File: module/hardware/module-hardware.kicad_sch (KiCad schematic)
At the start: 49 parts

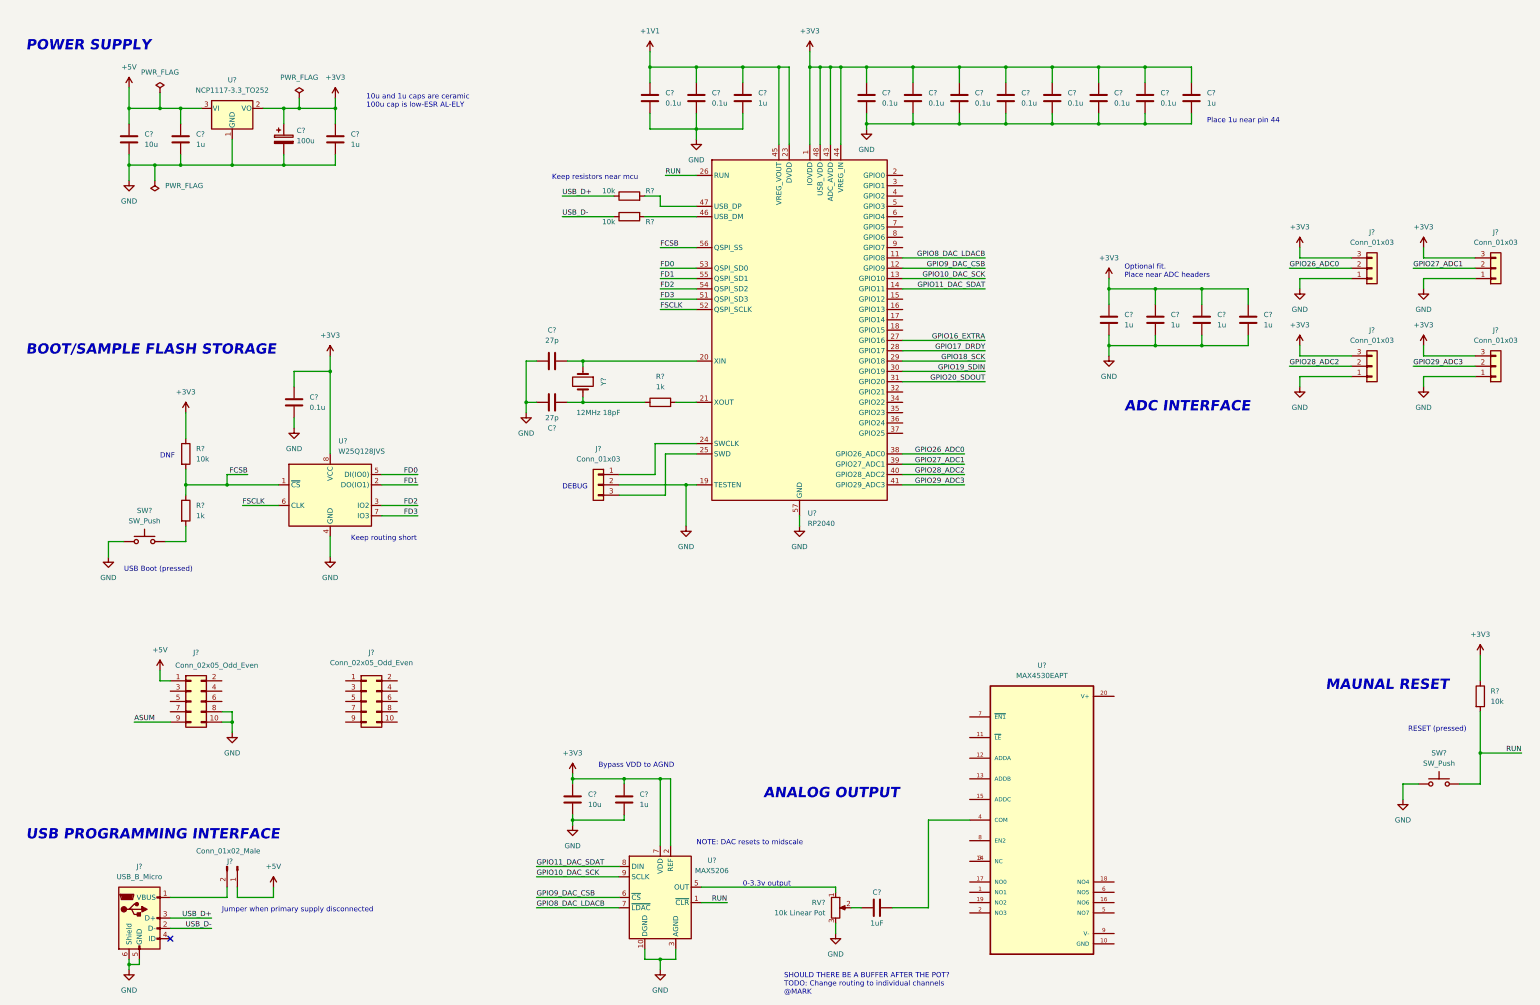
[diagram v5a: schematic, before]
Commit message: Isolated Analog & Digital GND
Also added coupling caps to sequencer mixer
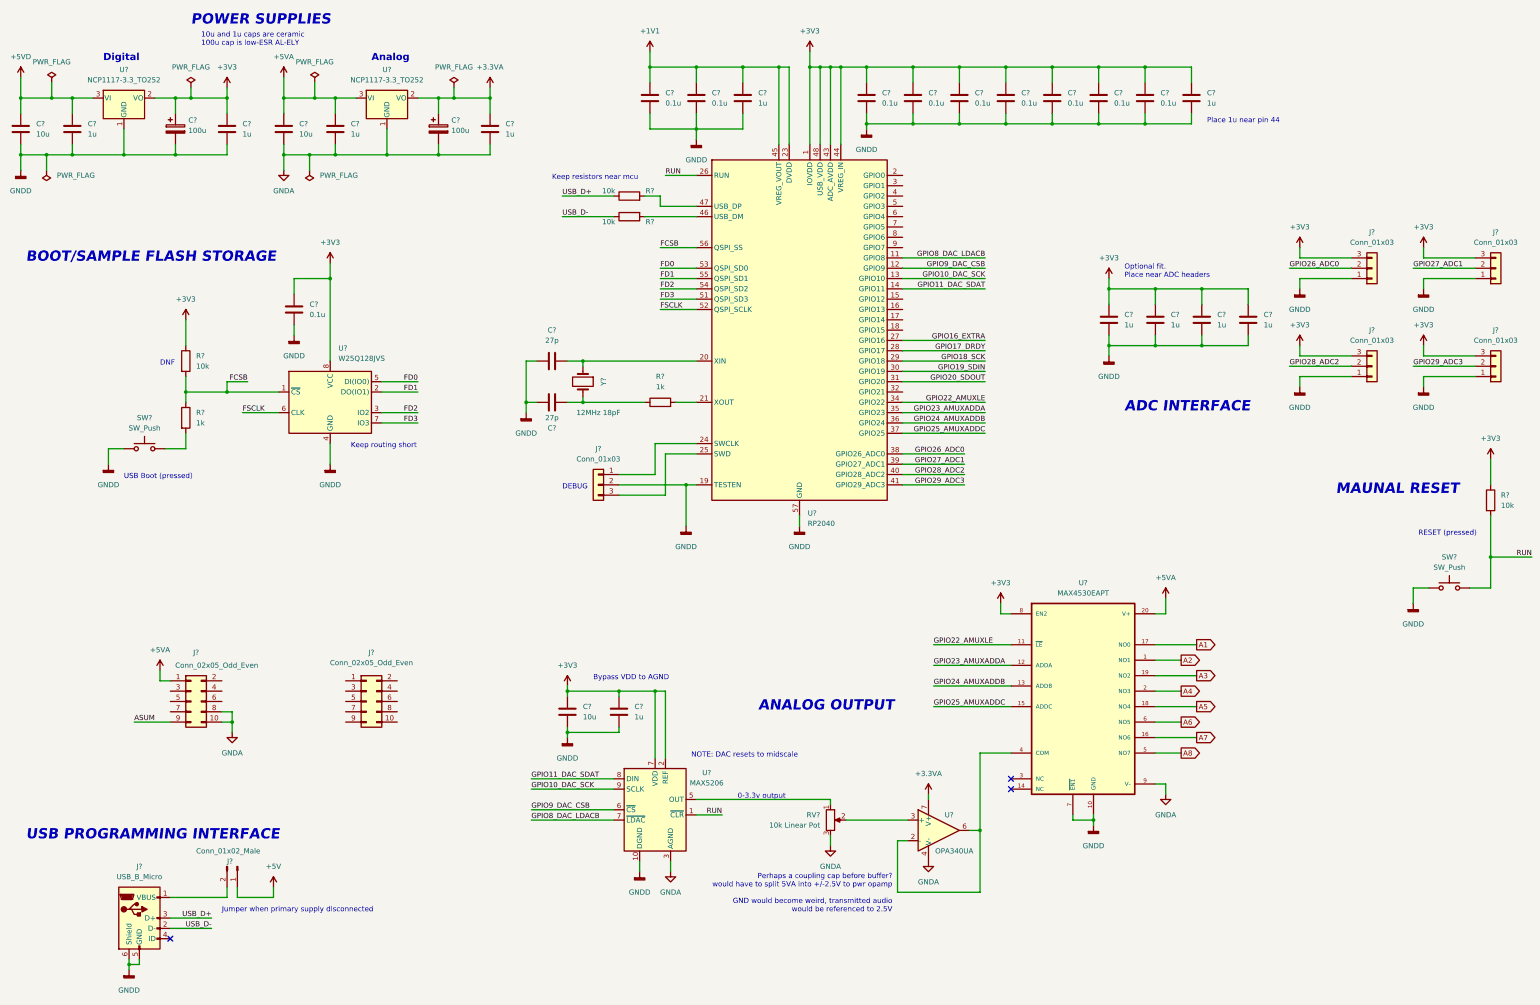
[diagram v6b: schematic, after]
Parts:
- removed C?: 1uF, symbol Device:C
- added C?: 100u, symbol Device:C_Polarized
- added C? (x2): 1u, symbol Device:C
- added C?: 10u, symbol Device:C
- added U?: NCP1117-3.3_TO252, Package_TO_SOT_SMD:TO-252-2, symbol Regulator_Linear:NCP1117-3.3_TO252
- added U?: OPA340UA, Package_SO:SOIC-8_3.9x4.9mm_P1.27mm, symbol Amplifier_Operational:OPA340UA
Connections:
- net +3V3: now also U?.8 (EN2)
- net +5V: no longer C?.1, C?.1, J?.1 (Pin_1), U?.3 (VI)
- net A2: now reaches U?.1 (NO1)
- net GNDD: now reaches U?.10 (GND)
- net GNDD: now also C?.1, C?.2, C?.2, C?.2, C?.2, C?.2, C?.2, C?.2, C?.2, C?.2, C?.2, C?.2, C?.2, C?.2, C?.2, C?.2, C?.2, C?.2, C?.2, C?.2, C?.2, C?.2, C?.2, C?.2, J?.1 (Pin_1), J?.1 (Pin_1), J?.1 (Pin_1), J?.1 (Pin_1), J?.2 (Pin_2), J?.5 (GND), J?.6 (Shield), SW?.1, SW?.1, U?.1 (GND), U?.10 (DGND), U?.19 (TESTEN), U?.4 (GND), U?.57 (GND), U?.7 (~{EN1})
- net GPIO22_AMUXLE: now reaches U?.11 (~{LE})
- net GPIO22_AMUXLE: now also U?.34 (GPIO22)
- net GPIO23_AMUXADDA: now reaches U?.12 (ADDA)
- net GPIO23_AMUXADDA: now also U?.35 (GPIO23)
- net GPIO24_AMUXADDB: now reaches U?.13 (ADDB)
- net GPIO24_AMUXADDB: now also U?.36 (GPIO24)
- net at U?.14 (NC): no longer U?.3 (NC)
- net GPIO25_AMUXADDC: now reaches U?.15 (ADDC)
- net GPIO25_AMUXADDC: now also U?.37 (GPIO25)
- net A7: now reaches U?.16 (NO6)
- net A1: now reaches U?.17 (NO0)
- net A5: now reaches U?.18 (NO4)
- net A3: now reaches U?.19 (NO2)
- net A4: now reaches U?.2 (NO3)
- net +5VA: now reaches U?.20 (V+)
- net +5VA: now also J?.1 (Pin_1), C?.1, C?.1, U?.3 (VI)
- net at U?.4 (COM): now also U?.2 (-), U?.6
- net A8: now reaches U?.5 (NO7)
- net A6: now reaches U?.6 (NO5)
- net GNDA: now reaches U?.9 (V-)
- net GNDA: now also J?.10 (Pin_10), J?.8 (Pin_8), RV?.3, U?.3 (AGND), C?.2, C?.2, C?.2, C?.2, U?.1 (GND), U?.4 (V-)
- net at RV?.2: now also U?.3 (+)
- removed net GND: C?.1, C?.2, C?.2, C?.2, C?.2, C?.2, C?.2, C?.2, C?.2, C?.2, C?.2, C?.2, C?.2, C?.2, C?.2, C?.2, C?.2, C?.2, C?.2, C?.2, C?.2, C?.2, C?.2, C?.2, J?.1 (Pin_1), J?.1 (Pin_1), J?.1 (Pin_1), J?.1 (Pin_1), J?.10 (Pin_10), J?.2 (Pin_2), J?.5 (GND), J?.6 (Shield), J?.8 (Pin_8), RV?.3, SW?.1, SW?.1, U?.1 (GND), U?.10 (DGND), U?.19 (TESTEN), U?.3 (AGND), U?.4 (GND), U?.57 (GND)
- new net +3.3VA: C?.1, C?.1, U?.2 (VO), U?.7 (V+)
- new net +5VD: C?.1, C?.1, U?.3 (VI)
- no-connect marks 1 -> 3
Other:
- note added: "Analog"
- note added: "Digital"
- note added: "POWER SUPPLIES"
- note added: "Perhaps a coupling cap before buffer? would have to split 5VA into +/-2.5V to pwr opamp GND would become weird, transmitted audio would be referenced to 2.5V"
- note removed: "POWER SUPPLY"
- note removed: "SHOULD THERE BE A BUFFER AFTER THE POT? TODO: Change routing to individual channels @MARK"
- moved on the sheet: C?, R?, RV?, SW?, U?

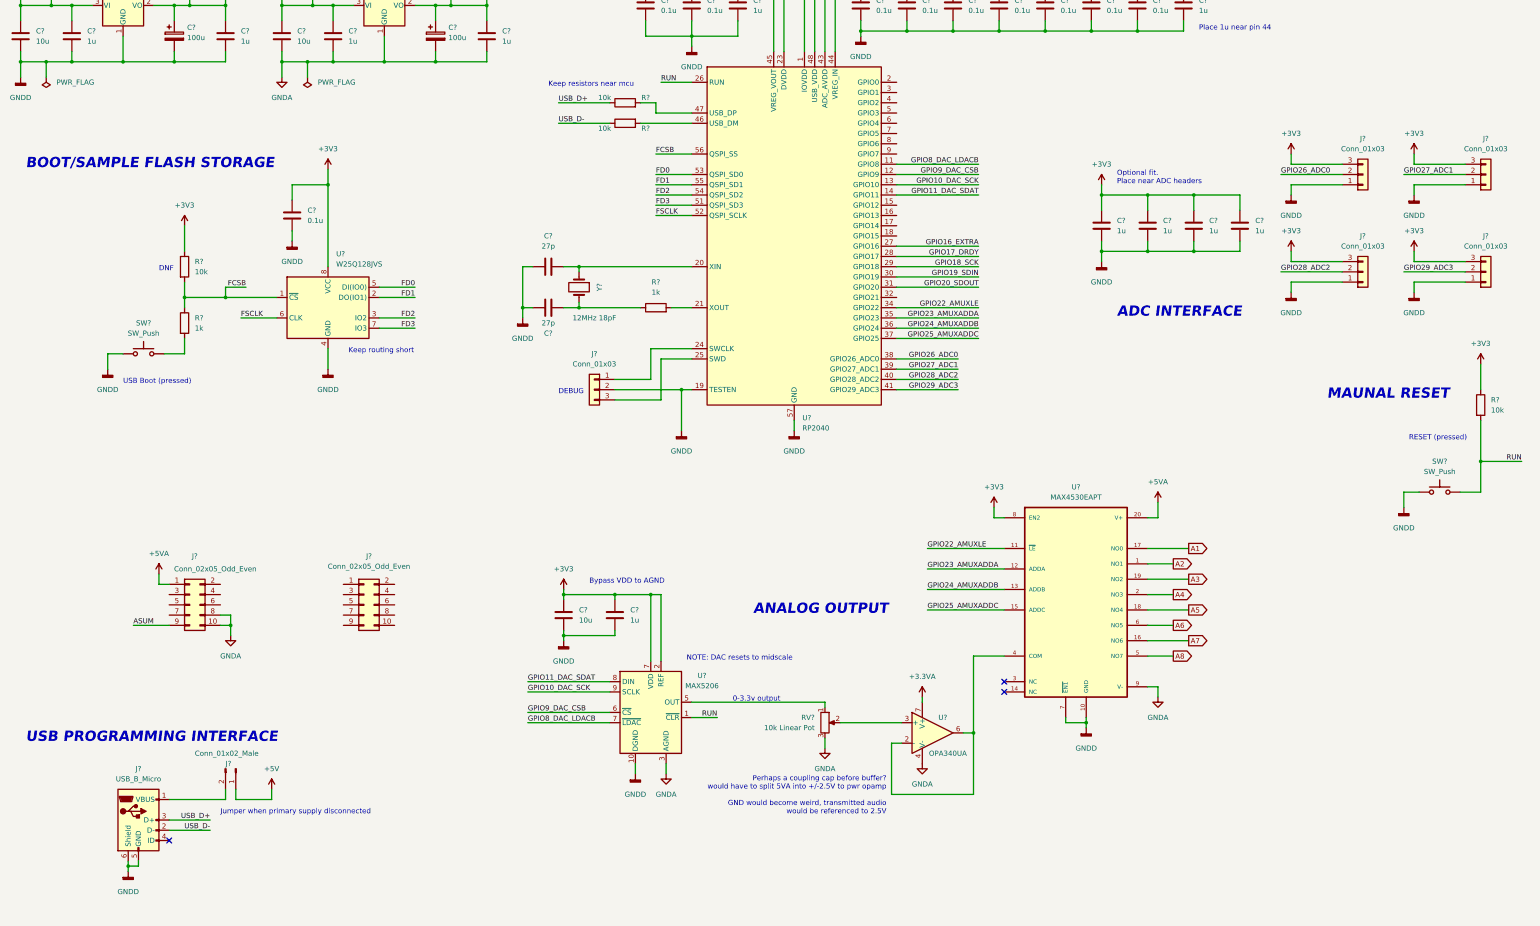
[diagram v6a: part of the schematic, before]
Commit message: Reworked audio routing to avoid MUX
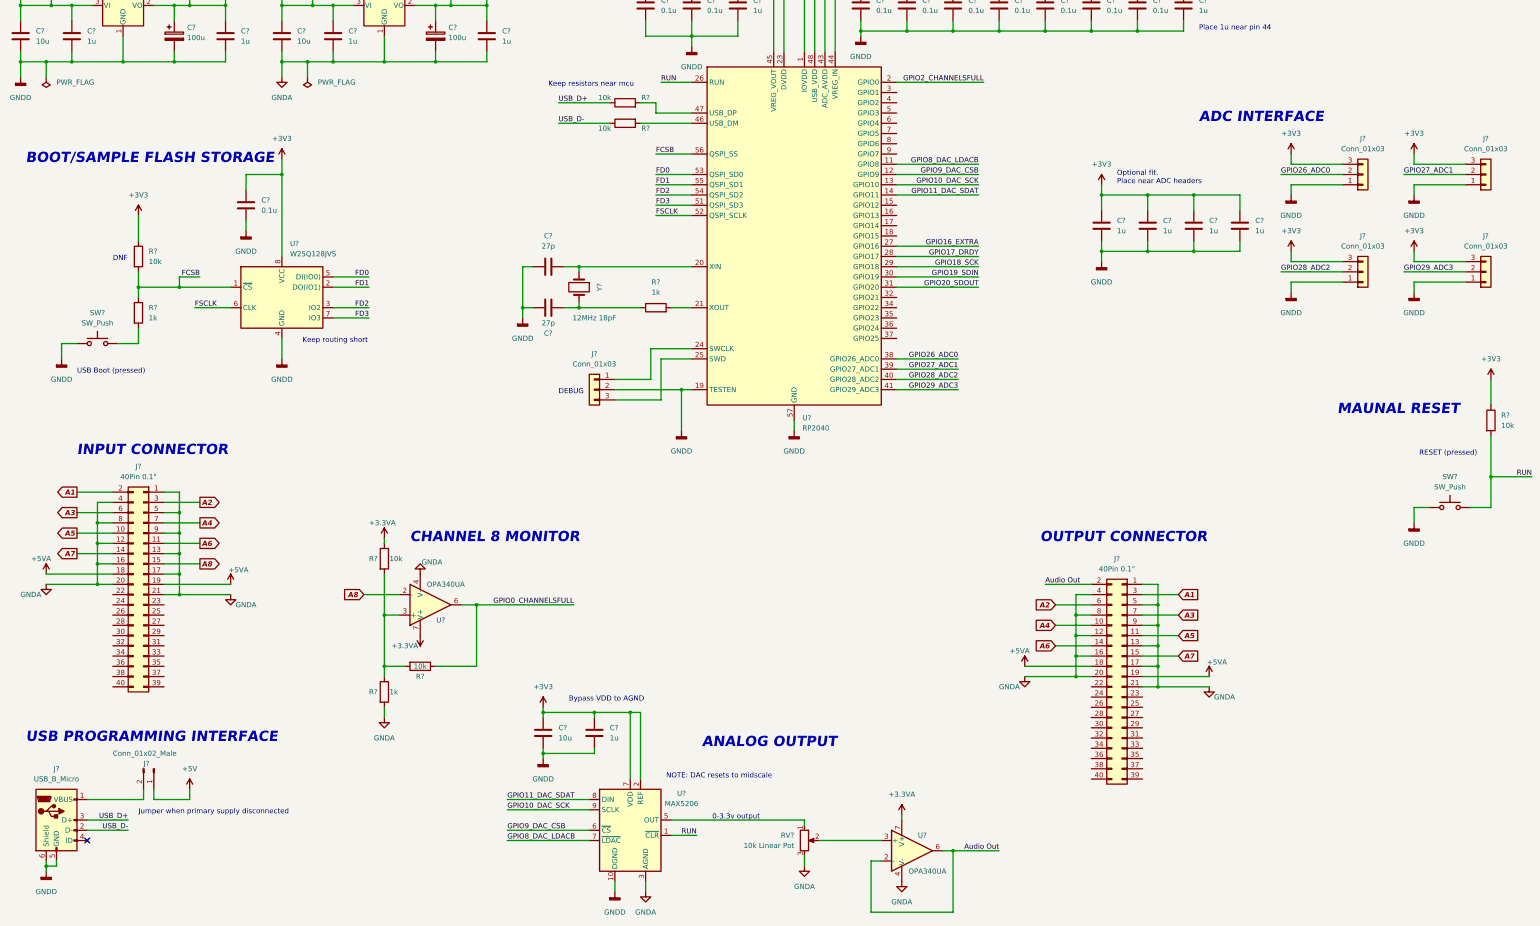
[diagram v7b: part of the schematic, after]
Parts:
- removed J? (x2): Conn_02x05_Odd_Even, symbol Connector_Generic:Conn_02x05_Odd_Even
- removed U?: MAX4530EAPT, SOP65P777X199-20N, symbol DRUM_Custom:MAX4530EAPT
- added J? (x2): 40Pin 0.1", symbol Connector_Generic:Conn_02x20_Odd_Even
- added R? (x2): 10k, symbol Device:R
- added R?: 1k, symbol Device:R
- added U?: OPA340UA, Package_SO:SOIC-8_3.9x4.9mm_P1.27mm, symbol Amplifier_Operational:OPA340UA
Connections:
- net +3.3VA: now also R?.1, U?.7 (V+)
- net +5VA: now also J?.18 (Pin_18), J?.18 (Pin_18), J?.19 (Pin_19), J?.19 (Pin_19)
- net A1: now also J?.2 (Pin_2), J?.3 (Pin_3)
- net A2: now also J?.3 (Pin_3), J?.6 (Pin_6)
- net A3: now also J?.6 (Pin_6), J?.7 (Pin_7)
- net A4: now also J?.10 (Pin_10), J?.7 (Pin_7)
- net A5: now also J?.10 (Pin_10), J?.11 (Pin_11)
- net A6: now also J?.11 (Pin_11), J?.14 (Pin_14)
- net A7: now also J?.14 (Pin_14), J?.15 (Pin_15)
- net A8: now also J?.15 (Pin_15), U?.2 (-)
- net GNDA: now also J?.1 (Pin_1), J?.1 (Pin_1), J?.12 (Pin_12), J?.12 (Pin_12), J?.13 (Pin_13), J?.13 (Pin_13), J?.16 (Pin_16), J?.16 (Pin_16), J?.17 (Pin_17), J?.17 (Pin_17), J?.20 (Pin_20), J?.20 (Pin_20), J?.21 (Pin_21), J?.21 (Pin_21), J?.4 (Pin_4), J?.4 (Pin_4), J?.5 (Pin_5), J?.5 (Pin_5), J?.8 (Pin_8), J?.8 (Pin_8), J?.9 (Pin_9), J?.9 (Pin_9), R?.2, U?.4 (V-)
- net Audio Out: now reaches U?.2 (-), U?.6
- net Audio Out: now also J?.2 (Pin_2)
- net GPIO2_CHANNELSFULL: now reaches U?.2 (GPIO0)
- net GPIO22_AMUXLE: no longer names the net of U?.34 (GPIO22)
- net GPIO23_AMUXADDA: no longer names the net of U?.35 (GPIO23)
- net GPIO24_AMUXADDB: no longer names the net of U?.36 (GPIO24)
- net GPIO25_AMUXADDC: no longer names the net of U?.37 (GPIO25)
- new net: R?.1, R?.2, R?.2, U?.3 (+)
- new net GPIO0_CHANNELSFULL: R?.1, U?.6
- no-connect marks 3 -> 1
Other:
- note added: "CHANNEL 8 MONITOR"
- note added: "INPUT CONNECTOR"
- note added: "OUTPUT CONNECTOR"
- note removed: "Perhaps a coupling cap before buffer? would have to split 5VA into +/-2.5V to pwr opamp GND would become weird, transmitted audio would be referenced to 2.5V"
- moved on the sheet: C?, J?, R?, RV?, SW?, U?

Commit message: Move digital to separate sheet
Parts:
- removed C? (x7): 1u, symbol Device:C
- removed C? (x10): 0.1u, symbol Device:C
- removed C? (x2): 27p, symbol Device:C
- removed C?: 10u, symbol Device:C
- removed J? (x5): Conn_01x03, symbol Connector_Generic:Conn_01x03
- removed R? (x3): 10k, symbol Device:R
- removed R? (x2): 1k, symbol Device:R
- removed SW?: SW_Push, symbol Switch:SW_Push
- removed U?: W25Q128JVS, Package_SO:SOIC-8_5.23x5.23mm_P1.27mm, symbol Memory_Flash:W25Q128JVS
- removed U?: RP2040, Package_DFN_QFN:QFN-56-1EP_7x7mm_P0.4mm_EP3.2x3.2mm, symbol MCU_RaspberryPi:RP2040
- removed U?: MAX5206, Package_SO:MSOP-10_3x3mm_P0.5mm, symbol custom-lib:MAX5206
- removed Y?: 12MHz 18pF, symbol Device:Crystal
- added C?: 1u, symbol Device:C
- added C?: 10u, symbol Device:C
- added U?: 74LVC2G53, symbol 74xGxx:74LVC2G53
- added U?: MAX5206, Package_SO:MSOP-10_3x3mm_P0.5mm, symbol custom-lib:MAX5206
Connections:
- net +5V is gone; now on net +5VD: J?.1 (Pin_1)
- net +3V3: now also C?.1, C?.1, U?.2 (REF), U?.7 (~{LDAC})
- net +5VD: now also J?.24 (Pin_24), J?.25 (Pin_25)
- net GNDA: now also U?.3 (AGND)
- net GNDD: now also J?.22 (Pin_22), J?.23 (Pin_23), J?.26 (Pin_26), J?.27 (Pin_27), J?.30 (Pin_30), J?.31 (Pin_31), J?.34 (Pin_34), J?.35 (Pin_35), J?.38 (Pin_38), J?.39 (Pin_39), C?.2, C?.2, U?.10 (DGND)
- net RUN: now also U?.1 (~{CLR})
- net at RV?.1: now also U?.5 (OUT)
- net GPIO0_CHANNELSFULL renamed CHANNEL_FULL
- new net DAC_CSB: U?.6 (~{CS})
- new net DAC_LDACB: U?.7 (~{LDAC})
- new net DAC_SCK: U?.9 (SCLK)
- new net DAC_SDAT: U?.8 (DIN)
- new net GND: U?.3 (GND), U?.4 (GND)
- new net VCC: U?.8 (VCC)
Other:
- added sheet D.R.U.M. Module Digital (digital.kicad_sch)
- note added: "NOTE: AGND and DGND must be tied together at this point"
- note removed: "ADC INTERFACE"
- note removed: "BOOT/SAMPLE FLASH STORAGE"
- note removed: "DEBUG"
- note removed: "DNF"
- note removed: "Keep resistors near mcu"
- note removed: "Keep routing short"
- note removed: "Optional fit. Place near ADC headers"
- note removed: "Place 1u near pin 44"
- note removed: "USB Boot (pressed)"
- moved on the sheet: J?, R?, RV?, SW?, U?
